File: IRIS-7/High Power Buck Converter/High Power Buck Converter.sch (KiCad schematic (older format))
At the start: 35 parts, among them IC1 LM5088-2, Q1 CSD19534Q5A

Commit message: Begin assiging footprints to schematic symbols
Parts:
- added C14, C15: 10uF, Capacitors_SMD:C_1206, symbol C
- C1, C2, C3, C4: footprint (none) -> Capacitors_SMD:C_0805
- C10: renamed from C?; footprint (none) -> Capacitors_SMD:C_1210
- C11: renamed from C9; footprint (none) -> Capacitors_SMD:C_1210
- C12, C13: renamed from C?; value 22uF -> 10uF; footprint (none) -> Capacitors_SMD:C_1206
- C16: renamed from C10; footprint (none) -> Capacitors_SMD:CP_Elec_8x10.5; symbol C -> CP
- C17: renamed from C11; footprint (none) -> Capacitors_SMD:CP_Elec_8x10.5; symbol C -> CP
- C5: renamed from C?; footprint (none) -> Capacitors_SMD:C_1210; symbol CP -> C; ESR 1.73m -> (none)
- C6: renamed from C5; footprint (none) -> Capacitors_SMD:C_1210; symbol CP -> C; ESR 1.73m -> (none)
- C7: renamed from C6; footprint (none) -> Capacitors_SMD:C_0805
- C8: renamed from C7; footprint (none) -> Capacitors_SMD:C_0805
- C9: renamed from C8; footprint (none) -> Capacitors_SMD:C_0805
- D1: footprint (none) -> TO_SOT_Packages_SMD:TO-263-3Lead
- JP1: footprint (none) -> Pin_Headers:Pin_Header_Straight_2x01_Pitch2.54mm
- JP2: footprint (none) -> Pin_Headers:Pin_Header_Straight_1x03_Pitch2.54mm
- L1: footprint (none) -> Buck_Converter:XAL1010
- R1, R10, R2, R3, R4, R5, R6, R7, R8, R9: footprint (none) -> Resistors_SMD:R_0805
- gave numbers to parts that had none: 4
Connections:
- net GND: now also C14.2, C15.2
- net Vout: now also C14.1, C15.1
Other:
- moved on the sheet: C1, C10, C11, C12, C13, C2, C3, C4, C7, C8, C9, D1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

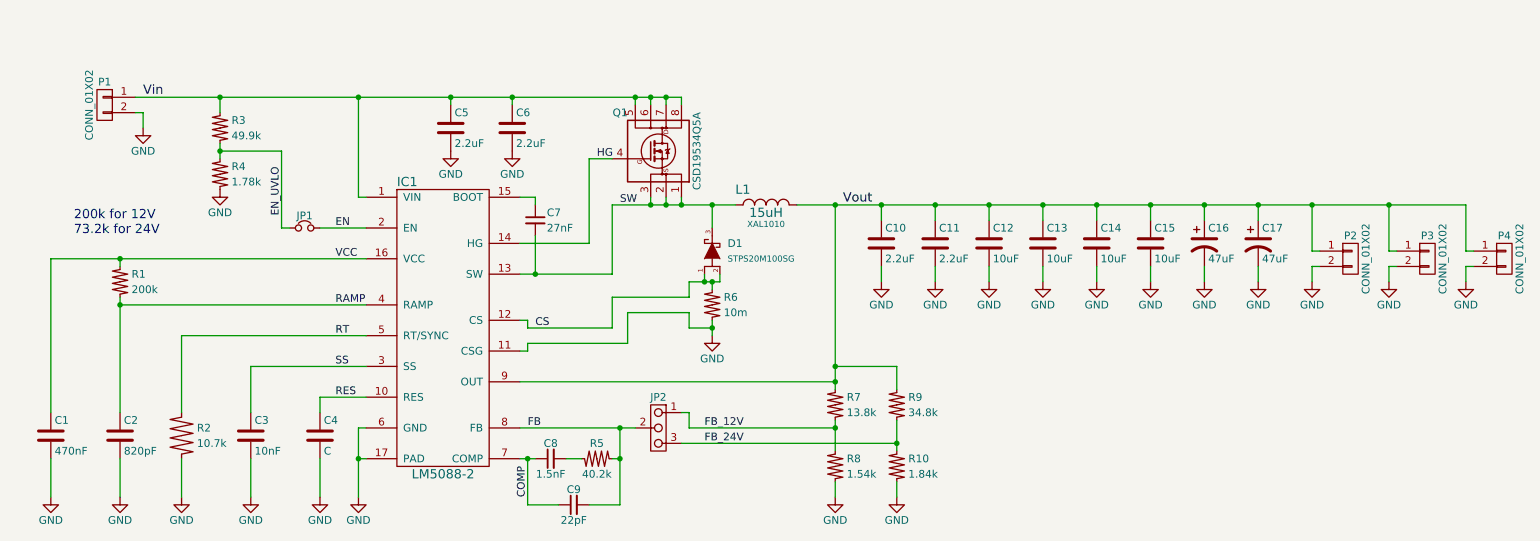
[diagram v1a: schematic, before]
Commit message: Finish assigning part footprints
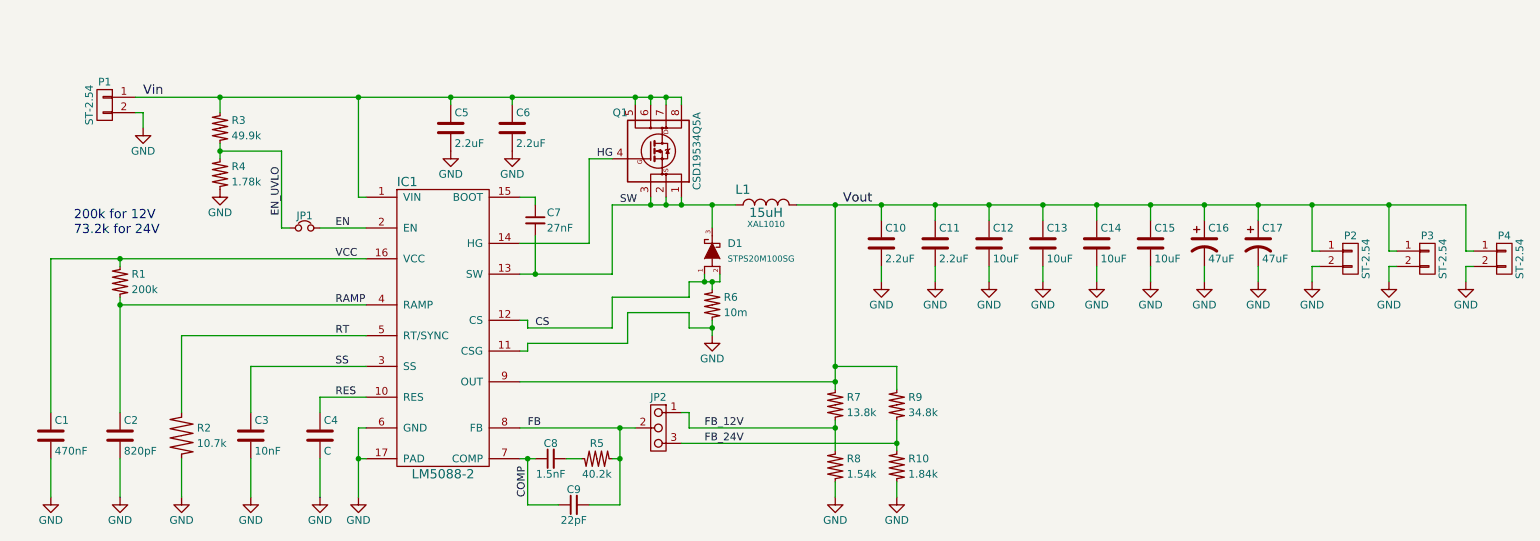
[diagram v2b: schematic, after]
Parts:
- IC1: footprint (none) -> Buck_Converter:HTSSOP-16_EP
- P1, P2, P3, P4: value CONN_01X02 -> ST-2.54; footprint (none) -> Terminal_Blocks:TerminalBlock_Pheonix_MPT-2.54mm_2pol
- Q1: footprint (none) -> TO_SOT_Packages_SMD:TDSON-8-1
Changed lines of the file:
@@
 F 0 "IC1" H 3100 5250 60  0000 L CNN
 F 1 "LM5088-2" H 3400 3350 60  0000 C CNN
-F 2 "" H 3700 3750 60  0001 C CNN
+F 2 "Buck_Converter:HTSSOP-16_EP" H 3700 3750 60  0001 C CNN
 F 3 "" H 3700 3750 60  0000 C CNN
 	1    3400 4250
@@
 F 0 "Q1" H 4600 3300 50  0000 R CNN
 F 1 "CSD19534Q5A" V 5050 3050 50  0000 C CNN
-F 2 "" V 4950 3050 50  0001 C CIN
+F 2 "TO_SOT_Packages_SMD:TDSON-8-1" V 4950 3050 50  0001 C CIN
 F 3 "" V 5050 2850 50  0000 L CNN
 	1    4800 3050
@@
 P 1200 2750
 F 0 "P1" H 1200 2900 50  0000 C CNN
-F 1 "CONN_01X02" V 1300 2750 50  0000 C CNN
-F 2 "" H 1200 2750 50  0001 C CNN
+F 1 "ST-2.54" V 1300 2750 50  0000 C CNN
+F 2 "Terminal_Blocks:TerminalBlock_Pheonix_MPT-2.54mm_2pol" H 1200 2750 50  0001 C CNN
 F 3 "" H 1200 2750 50  0000 C CNN
 	1    1200 2750
@@
 P 9300 3750
 F 0 "P2" H 9300 3900 50  0000 C CNN
-F 1 "CONN_01X02" V 9400 3750 50  0000 C CNN
-F 2 "" H 9300 3750 50  0001 C CNN
+F 1 "ST-2.54" V 9400 3750 50  0000 C CNN
+F 2 "Terminal_Blocks:TerminalBlock_Pheonix_MPT-2.54mm_2pol" H 9300 3750 50  0001 C CNN
 F 3 "" H 9300 3750 50  0000 C CNN
 	1    9300 3750
@@
 P 9800 3750
 F 0 "P3" H 9800 3900 50  0000 C CNN
-F 1 "CONN_01X02" V 9900 3750 50  0000 C CNN
-F 2 "" H 9800 3750 50  0001 C CNN
+F 1 "ST-2.54" V 9900 3750 50  0000 C CNN
+F 2 "Terminal_Blocks:TerminalBlock_Pheonix_MPT-2.54mm_2pol" H 9800 3750 50  0001 C CNN
 F 3 "" H 9800 3750 50  0000 C CNN
 	1    9800 3750
@@
 P 10300 3750
 F 0 "P4" H 10300 3900 50  0000 C CNN
-F 1 "CONN_01X02" V 10400 3750 50  0000 C CNN
-F 2 "" H 10300 3750 50  0001 C CNN
+F 1 "ST-2.54" V 10400 3750 50  0000 C CNN
+F 2 "Terminal_Blocks:TerminalBlock_Pheonix_MPT-2.54mm_2pol" H 10300 3750 50  0001 C CNN
 F 3 "" H 10300 3750 50  0000 C CNN
 	1    10300 3750

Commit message: Begin component placement
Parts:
- D1: symbol D_Schottky_2Anode -> D_Schottky_AKA
- JP1: footprint Pin_Headers:Pin_Header_Straight_2x01_Pitch2.54mm -> Pin_Headers:Pin_Header_Straight_1x02_Pitch2.54mm
- R6: footprint Resistors_SMD:R_0805 -> Resistors_SMD:R_2010
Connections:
- net CS: now also D1.3 (A); no longer D1.2 (A)
- net SW: now also D1.2 (K); no longer D1.3 (K)
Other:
- note added: "TODO:\nUpdate diode footprint to remove extra pin 2"
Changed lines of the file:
@@
 LIBS:TI
 LIBS:Transistor
+LIBS:Buck_Converter
 LIBS:High Power Buck Converter-cache
 EELAYER 25 0
@@
 $EndComp
 $Comp
-L D_Schottky_2Anode D1
+L D_Schottky_AKA D1
 U 1 1 58B6402B
 P 5150 3700
@@
 F 0 "R6" H 5225 4100 50  0000 L CNN
 F 1 "10m" H 5225 4000 50  0000 L CNN
-F 2 "Resistors_SMD:R_0805" V 5150 4050 50  0001 C CNN
+F 2 "Resistors_SMD:R_2010" V 5150 4050 50  0001 C CNN
 F 3 "" V 5150 4050 50  0000 C CNN
 	1    5150 4050
@@
 F 0 "JP1" H 2500 3630 50  0000 C CNN
 F 1 "JP_NC" H 2510 3490 50  0001 C CNN
-F 2 "Pin_Headers:Pin_Header_Straight_2x01_Pitch2.54mm" H 2500 3550 50  0001 C CNN
+F 2 "Pin_Headers:Pin_Header_Straight_1x02_Pitch2.54mm" H 2500 3550 50  0001 C CNN
 F 3 "" H 2500 3550 50  0000 C CNN
 	1    2500 3550
@@
 Connection ~ 7650 3400
 Connection ~ 8000 3400
+Text Notes 5400 2950 0    60   ~ 0
+TODO:\nUpdate diode footprint to remove extra pin 2
 $EndSCHEMATC

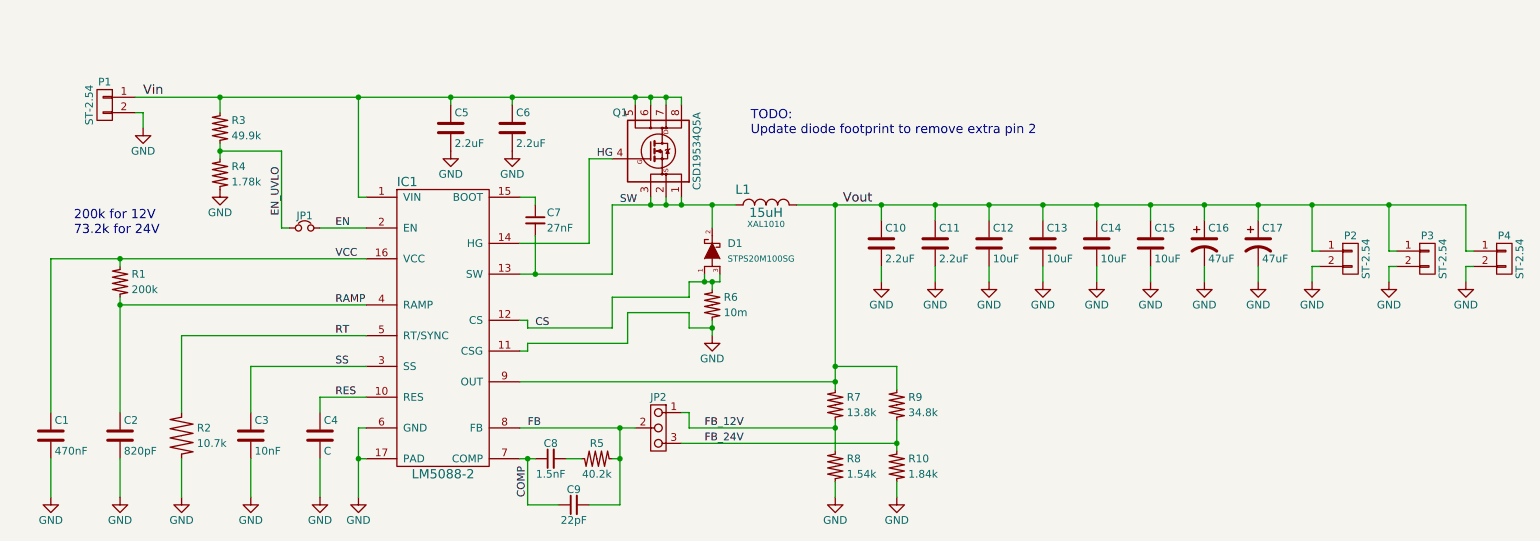
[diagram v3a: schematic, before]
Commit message: Update power routing
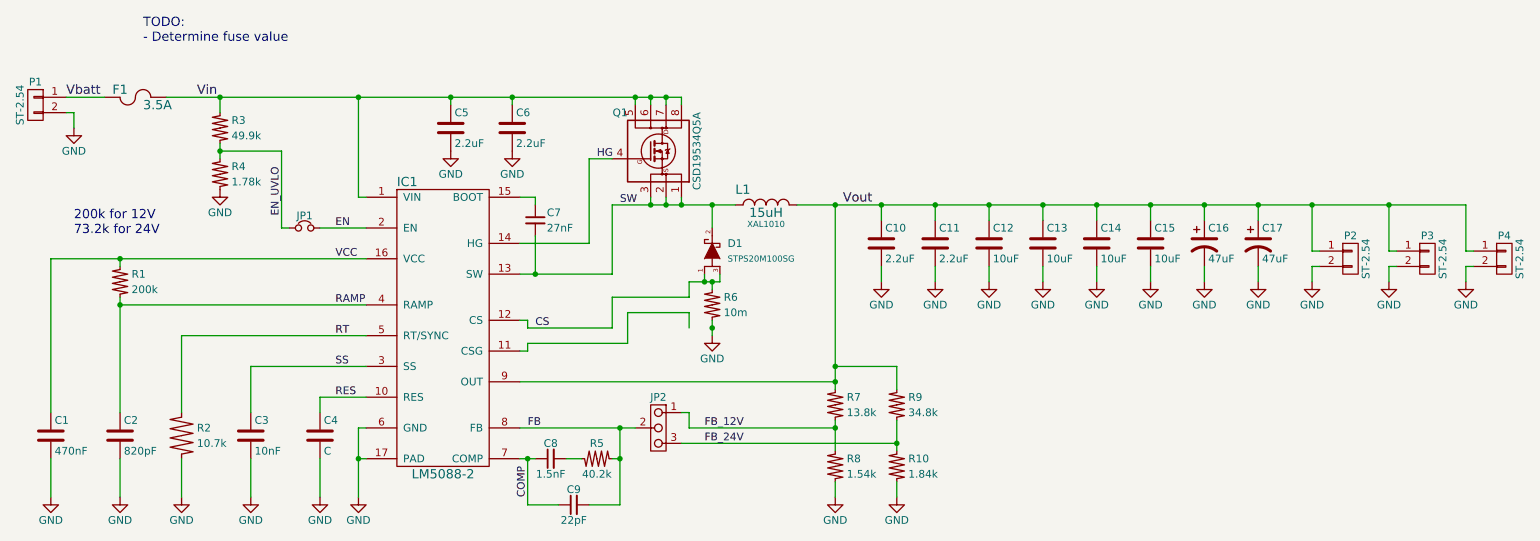
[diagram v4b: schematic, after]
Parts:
- added F1: 3.5A, Fuse_Holders_and_Fuses:Fuseholder5x20_horiz_open_Schurter_0031_8201, symbol F
- P1, P2, P3, P4: footprint Terminal_Blocks:TerminalBlock_Pheonix_MPT-2.54mm_2pol -> Terminal_Blocks:TerminalBlock_Pheonix_MKDS1.5-2pol
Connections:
- net GND: no longer IC1.11 (CSG)
- net Vin: now also F1.2; no longer P1.1 (P1)
- new net Vbatt: F1.1, P1.1 (P1)
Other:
- note added: "TODO:\n- Determine fuse value"
- note removed: "TODO:\nUpdate diode footprint to remove extra pin 2"
- moved on the sheet: P1
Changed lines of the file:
@@
 	5000 4100 5000 4200
-Wire Wire Line
-	5000 4200 5150 4200
 Wire Wire Line
 	3950 5050 3950 5350
@@
 	4950 2700 4950 2750
 Wire Wire Line
-	1400 2700 4950 2700
+	1600 2700 4950 2700
 Wire Wire Line
 	4650 2750 4650 2700
@@
 L CONN_01X02 P1
 U 1 1 58EC4787
-P 1200 2750
-F 0 "P1" H 1200 2900 50  0000 C CNN
-F 1 "ST-2.54" V 1300 2750 50  0000 C CNN
-F 2 "Terminal_Blocks:TerminalBlock_Pheonix_MPT-2.54mm_2pol" H 1200 2750 50  0001 C CNN
-F 3 "" H 1200 2750 50  0000 C CNN
-	1    1200 2750
+P 750 2750
+F 0 "P1" H 750 2900 50  0000 C CNN
+F 1 "ST-2.54" V 850 2750 50  0000 C CNN
+F 2 "Terminal_Blocks:TerminalBlock_Pheonix_MKDS1.5-2pol" H 750 2750 50  0001 C CNN
+F 3 "" H 750 2750 50  0000 C CNN
+	1    750  2750
 	-1   0    0    -1
 $EndComp
@@
 Wire Wire Line
 	2350 3550 2350 3050
-Text Label 1450 2700 0    60   ~ 0
+Text Label 1800 2700 0    60   ~ 0
 Vin
 $Comp
 L GND #PWR019
 U 1 1 58EC76BE
-P 1450 2900
-F 0 "#PWR019" H 1450 2650 50  0001 C CNN
-F 1 "GND" H 1450 2750 50  0000 C CNN
-F 2 "" H 1450 2900 50  0000 C CNN
-F 3 "" H 1450 2900 50  0000 C CNN
-	1    1450 2900
-	1    0    0    -1
-$EndComp
-Wire Wire Line
-	1450 2900 1450 2800
-Wire Wire Line
-	1450 2800 1400 2800
+P 1000 2900
+F 0 "#PWR019" H 1000 2650 50  0001 C CNN
+F 1 "GND" H 1000 2750 50  0000 C CNN
+F 2 "" H 1000 2900 50  0000 C CNN
+F 3 "" H 1000 2900 50  0000 C CNN
+	1    1000 2900
+	1    0    0    -1
+$EndComp
+Wire Wire Line
+	1000 2900 1000 2800
+Wire Wire Line
+	1000 2800 950  2800
 $Comp
 L CONN_01X02 P2
@@
 F 0 "P2" H 9300 3900 50  0000 C CNN
 F 1 "ST-2.54" V 9400 3750 50  0000 C CNN
-F 2 "Terminal_Blocks:TerminalBlock_Pheonix_MPT-2.54mm_2pol" H 9300 3750 50  0001 C CNN
+F 2 "Terminal_Blocks:TerminalBlock_Pheonix_MKDS1.5-2pol" H 9300 3750 50  0001 C CNN
 F 3 "" H 9300 3750 50  0000 C CNN
 	1    9300 3750
@@
 F 0 "P3" H 9800 3900 50  0000 C CNN
 F 1 "ST-2.54" V 9900 3750 50  0000 C CNN
-F 2 "Terminal_Blocks:TerminalBlock_Pheonix_MPT-2.54mm_2pol" H 9800 3750 50  0001 C CNN
+F 2 "Terminal_Blocks:TerminalBlock_Pheonix_MKDS1.5-2pol" H 9800 3750 50  0001 C CNN
 F 3 "" H 9800 3750 50  0000 C CNN
 	1    9800 3750
@@
 F 0 "P4" H 10300 3900 50  0000 C CNN
 F 1 "ST-2.54" V 10400 3750 50  0000 C CNN
-F 2 "Terminal_Blocks:TerminalBlock_Pheonix_MPT-2.54mm_2pol" H 10300 3750 50  0001 C CNN
+F 2 "Terminal_Blocks:TerminalBlock_Pheonix_MKDS1.5-2pol" H 10300 3750 50  0001 C CNN
 F 3 "" H 10300 3750 50  0000 C CNN
 	1    10300 3750
@@
 Connection ~ 7650 3400
 Connection ~ 8000 3400
-Text Notes 5400 2950 0    60   ~ 0
-TODO:\nUpdate diode footprint to remove extra pin 2
+$Comp
+L F F1
+U 1 1 58FC1075
+P 1400 2700
+F 0 "F1" H 1300 2750 60  0000 C CNN
+F 1 "3.5A" H 1450 2650 60  0000 L CNN
+F 2 "Fuse_Holders_and_Fuses:Fuseholder5x20_horiz_open_Schurter_0031_8201" H 1400 2700 60  0001 C CNN
+F 3 "" H 1400 2700 60  0000 C CNN
+	1    1400 2700
+	1    0    0    -1
+$EndComp
+Wire Wire Line
+	1200 2700 950  2700
+Text Label 950  2700 0    60   ~ 0
+Vbatt
+Text Notes 1450 2350 0    60   ~ 0
+TODO:\n- Determine fuse value
 $EndSCHEMATC

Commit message: Finish layout and final tweaks
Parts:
- added D2: Blue, LEDs:LED_0805, symbol Led_Small
- added J1: GND, Buck_Converter:SMD_0.3, symbol TEST_1P
- added J2: CS_P, Buck_Converter:SMD_0.3, symbol TEST_1P
- added R11: 34.8k, Resistors_SMD:R_0805, symbol R_Small
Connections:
- net GND: now also D2.1 (K)
- net Vout: now also R11.2
- net CS_N: now reaches IC1.11 (CSG)
- net CS_N: now also J1.1
- net CS renamed CS_P
- net CS_P: now also J2.1
- new net: D2.2 (A), R11.1
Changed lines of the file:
@@
 COMP
 Text Label 4000 4200 0    50   ~ 0
-CS
+CS_P
 Text Label 4550 3400 0    50   ~ 0
 SW
@@
 	5100 3850 5100 3900
 Wire Wire Line
-	5000 3900 5200 3900
+	4950 3900 5200 3900
 Wire Wire Line
 	5150 3900 5150 3950
@@
 Text Notes 1450 2350 0    60   ~ 0
 TODO:\n- Determine fuse value
+Text Label 4000 4300 0    50   ~ 0
+CS_N
+$Comp
+L TEST_1P J1
+U 1 1 58FEBD32
+P 5000 4200
+F 0 "J1" H 5000 4470 50  0000 C CNN
+F 1 "GND" H 5000 4400 50  0000 C CNN
+F 2 "Buck_Converter:SMD_0.3" H 5200 4200 50  0001 C CNN
+F 3 "" H 5200 4200 50  0001 C CNN
+	1    5000 4200
+	0    -1   -1   0
+$EndComp
+$Comp
+L TEST_1P J2
+U 1 1 58FECFB2
+P 4950 3900
+F 0 "J2" H 4950 4170 50  0000 C CNN
+F 1 "CS_P" H 4950 4100 50  0000 C CNN
+F 2 "Buck_Converter:SMD_0.3" H 5150 3900 50  0001 C CNN
+F 3 "" H 5150 3900 50  0001 C CNN
+	1    4950 3900
+	0    -1   -1   0
+$EndComp
+Connection ~ 5000 3900
+$Comp
+L R_Small R11
+U 1 1 58FEF7F4
+P 9650 4650
+F 0 "R11" H 9725 4700 50  0000 L CNN
+F 1 "34.8k" H 9725 4600 50  0000 L CNN
+F 2 "Resistors_SMD:R_0805" V 9650 4650 50  0001 C CNN
+F 3 "" V 9650 4650 50  0000 C CNN
+	1    9650 4650
+	1    0    0    -1
+$EndComp
+$Comp
+L Led_Small D2
+U 1 1 58FEFBCC
+P 9650 4950
+F 0 "D2" V 9700 4850 50  0000 R CNN
+F 1 "Blue" V 9600 4850 50  0000 R CNN
+F 2 "LEDs:LED_0805" V 9650 4950 50  0001 C CNN
+F 3 "" V 9650 4950 50  0000 C CNN
+	1    9650 4950
+	0    -1   -1   0
+$EndComp
+Wire Wire Line
+	9650 4750 9650 4850
+$Comp
+L GND #PWR025
+U 1 1 58FF0287
+P 9650 5050
+F 0 "#PWR025" H 9650 4800 50  0001 C CNN
+F 1 "GND" H 9650 4900 50  0000 C CNN
+F 2 "" H 9650 5050 50  0001 C CNN
+F 3 "" H 9650 5050 50  0001 C CNN
+	1    9650 5050
+	1    0    0    -1
+$EndComp
+Wire Wire Line
+	9650 4550 9650 4450
+Wire Wire Line
+	9650 4450 9250 4450
+Text Label 9250 4450 0    60   ~ 0
+Vout
 $EndSCHEMATC
